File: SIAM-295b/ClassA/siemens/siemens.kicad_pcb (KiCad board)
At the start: 2 copper layers, 100 x 100 mm, 107 parts, among them J1 PWR_IN, J2 Conn_01x08_Pin, J3 AUDIO_IN, J4 AUDIO_OUT, Q1 BC849, Q10 BCX56, Q11 BCX56, Q12 BC849, Q2 BCX56, Q3 BCX56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

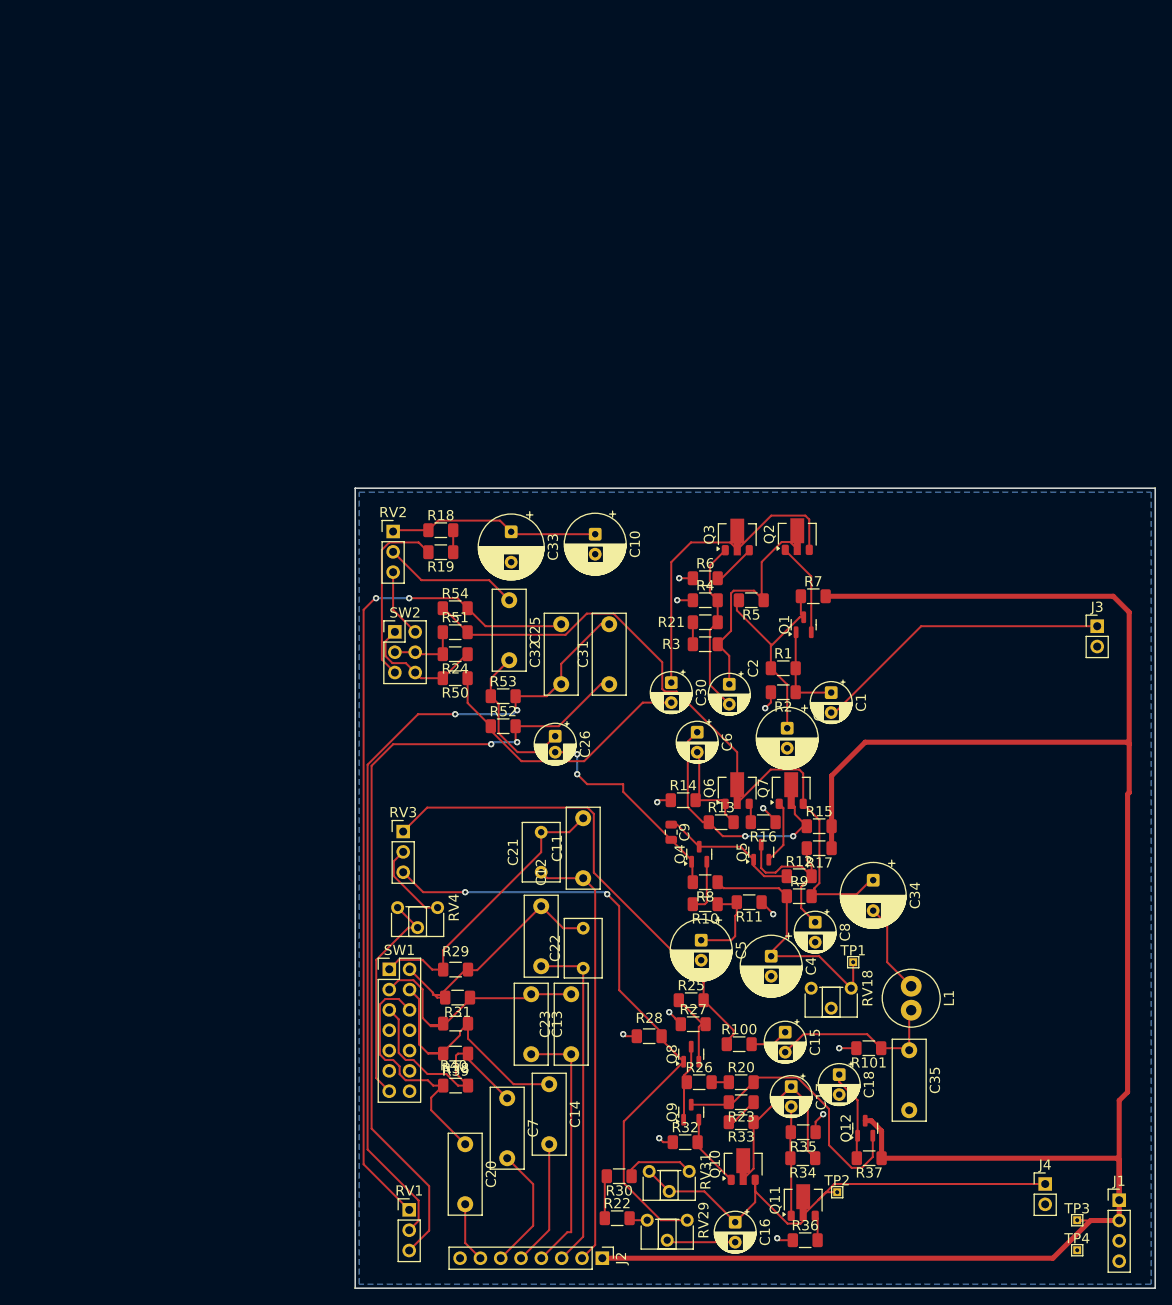
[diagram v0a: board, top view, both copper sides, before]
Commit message: update ocb
added mounting holes, reduced width
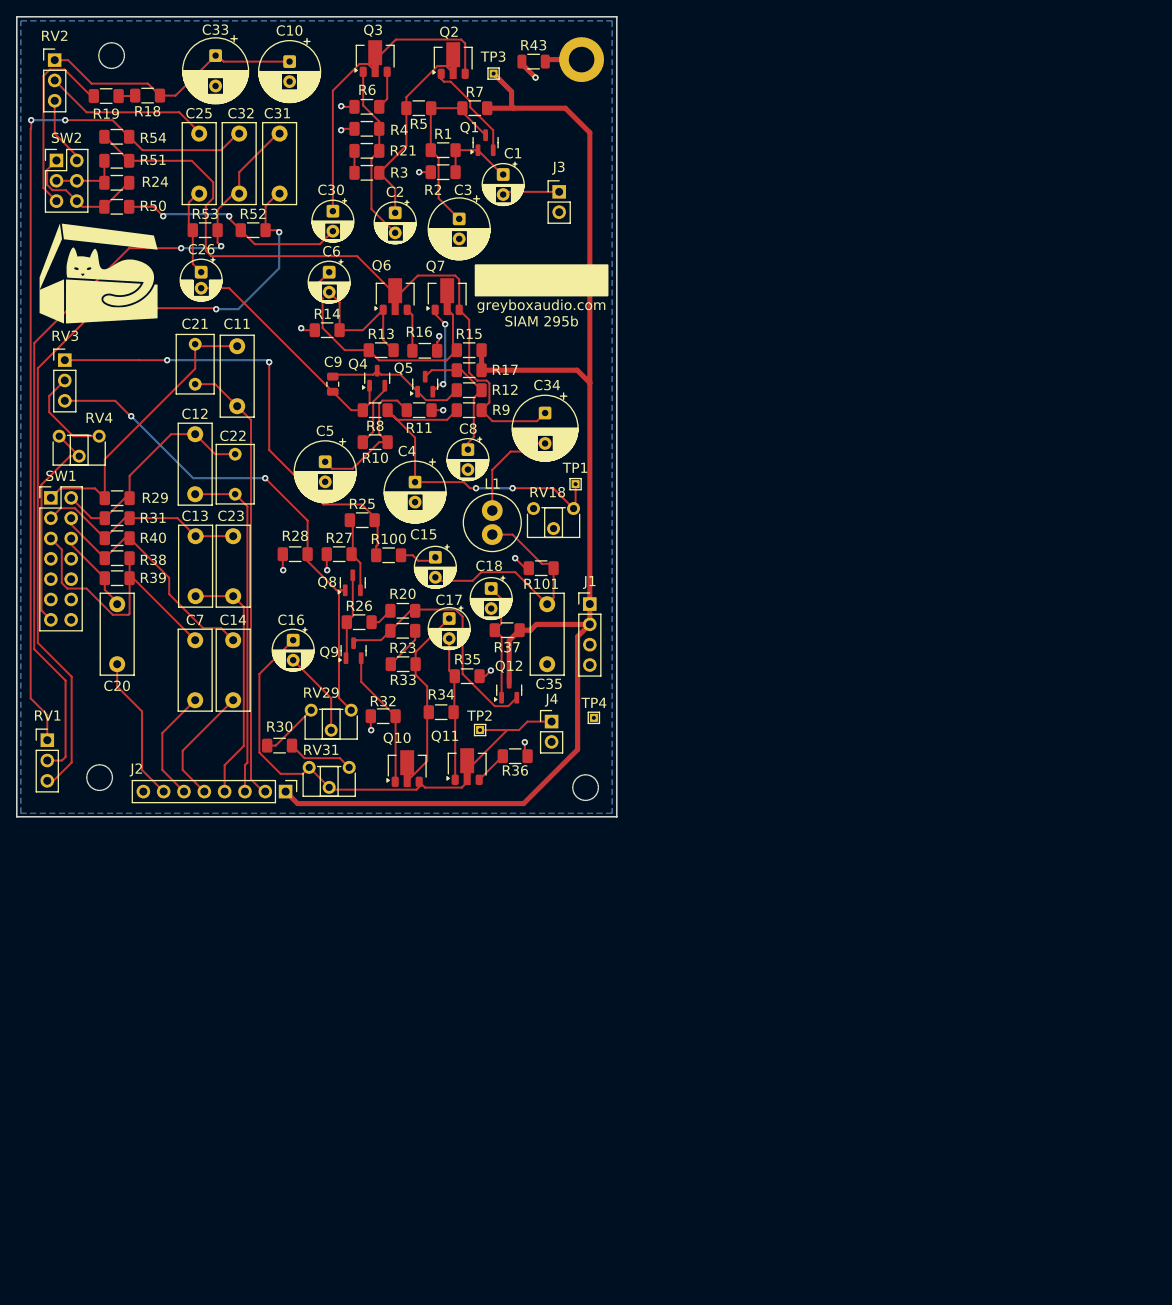
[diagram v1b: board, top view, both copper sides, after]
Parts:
- removed R22: 1k2, Resistor_SMD:R_1206_3216Metric_Pad1.30x1.75mm_HandSolder
- added G***: LOGO, LOGO, F.Cu at (35.8, 57.5)
- added H1: MountingHole, MountingHole:MountingHole_3.2mm_M3_DIN965, F.Cu at (37.2, 30.2)
- added H2: MountingHole, MountingHole:MountingHole_3.2mm_M3_DIN965, F.Cu at (35.8, 120.5)
- added H3: MountingHole, MountingHole:MountingHole_3.2mm_M3_DIN965_Pad, F.Cu at (96.0, 30.8)
- added H4: MountingHole, MountingHole:MountingHole_3.2mm_M3_DIN965, F.Cu at (96.5, 121.8)
- added R43: 0R, Resistor_SMD:R_1206_3216Metric, F.Cu at (90.0, 31.0)
- R18: value 1k3 -> 2k4
- R19: value 1k2 -> 100R
- R30: value 1k2 -> 2k4
- moved TP3 160.8 mm to (85.0, 32.5)
- moved J1 99.7 mm to (97.0, 98.8)
- moved C16 91.4 mm to (59.9, 103.3)
- moved TP4 89.9 mm to (97.5, 113.0)
- moved J3 86.4 mm to (93.2, 47.3)
- moved J4 84.5 mm to (92.2, 113.5)
- moved C20 80.3 mm to (37.9, 98.8)
- moved R37 80.0 mm to (86.7, 102.1)
- moved L1 79.2 mm to (84.8, 87.1)
- moved R2 77.7 mm to (78.7, 44.8)
- moved R1 77.5 mm to (78.7, 42.1)
- moved C1 76.6 mm to (86.2, 45.1)
- moved RV29 76.3 mm to (67.2, 112.1)
- moved R39 76.2 mm to (37.9, 95.6)
- moved C5 76.1 mm to (63.9, 81.0)
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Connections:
- R30 pad 2: Net-(R22-Pad1) -> Net-(R30-Pad2)
- RV29 pad 3: Net-(R22-Pad2) -> Net-(R30-Pad2)
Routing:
- net +24V: track 276.0 -> 170.0 mm
- net Net-(J3-Pin_1): track 37.3 -> 6.67 mm
- net Net-(C20-Pad1): track 30.6 -> 10.3 mm
- net Net-(Q8-B): track 78.8 -> 63.4 mm
- net Net-(C4-Pad1): track 31.8 -> 43.0 mm, vias 0 -> 2
- net Net-(J2-Pin_7): track 7.54 -> 18.3 mm
- net Net-(C25-Pad2): track 19.4 -> 10.2 mm
- net Net-(Q10-B): track 8.60 -> 17.2 mm
- net Net-(C15-Pad2): track 21.7 -> 29.9 mm
- net Net-(C5-Pad1): track 10.9 -> 18.9 mm
- net Net-(C10-Pad1): track 25.9 -> 33.3 mm
- net Net-(R30-Pad2): track 0.00 -> 7.33 mm
- net Net-(C30-Pad2): track 34.4 -> 28.5 mm, vias 0 -> 2
- net Net-(Q6-B): track 11.9 -> 17.4 mm
- net Net-(C7-Pad1): track 29.1 -> 34.2 mm
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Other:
- board size 100 x 100 mm -> 75 x 100 mm
- board text added: "greyboxaudio.com SIAM 295b"

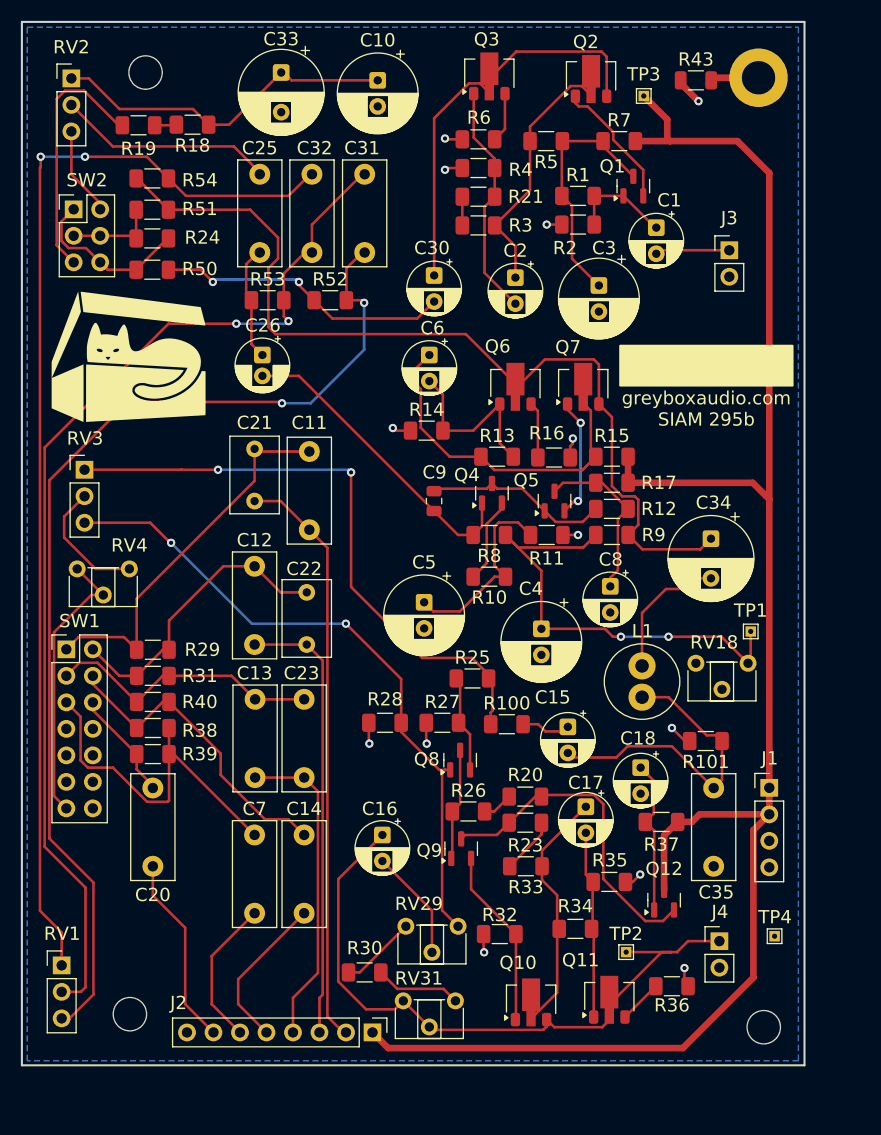
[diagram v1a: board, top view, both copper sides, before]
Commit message: update & fab
updated pcb, added fabrication output
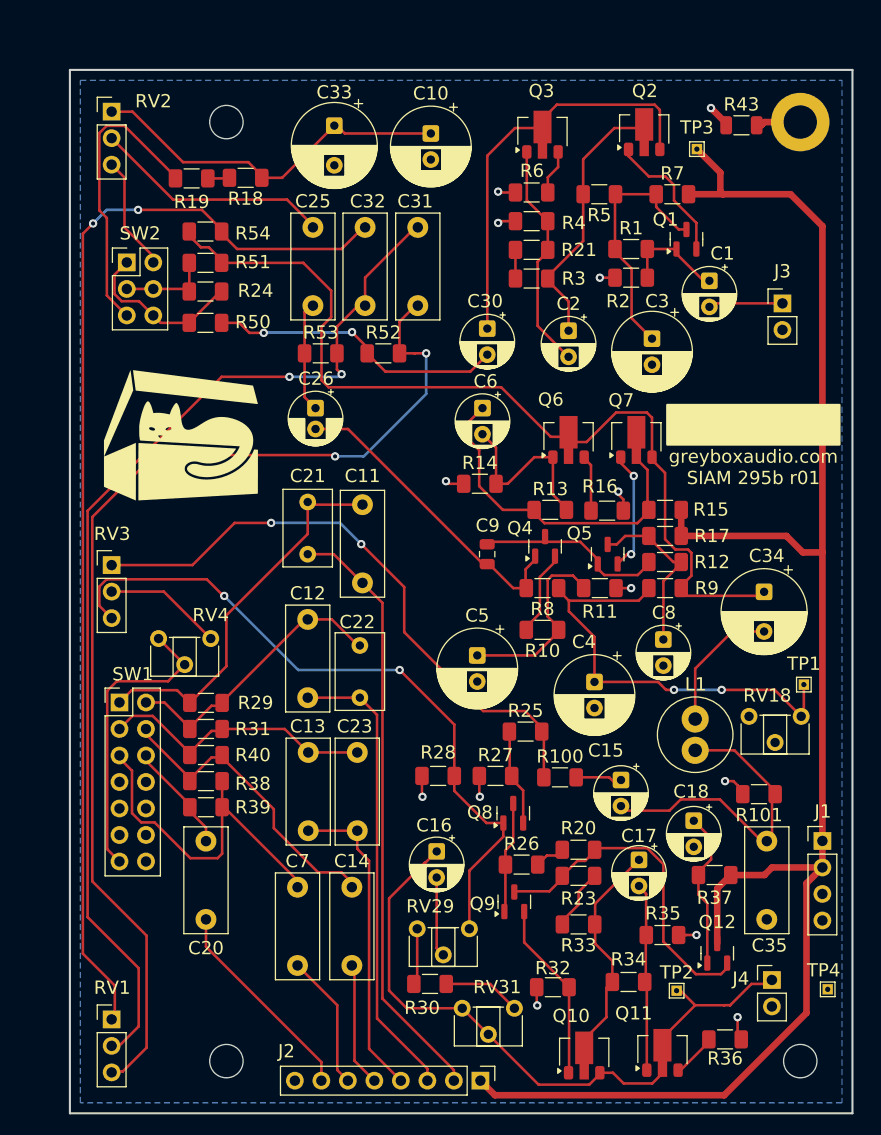
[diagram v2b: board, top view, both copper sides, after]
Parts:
- moved J2 11.3 mm to (69.3, 126.9)
- moved H2 10.3 mm to (45.0, 125.0)
- moved RV4 10.3 mm to (43.5, 84.5)
- moved RV3 9.50 mm to (34.0, 77.5)
- moved H1 9.09 mm to (45.0, 35.0)
- moved G*** 9.04 mm to (40.8, 65.0)
- moved Q3 7.56 mm to (75.3, 35.9)
- moved R33 7.52 mm to (78.8, 111.9)
- moved R100 7.20 mm to (77.0, 97.8)
- moved TP1 7.20 mm to (100.3, 88.9)
- moved C11 7.20 mm to (58.0, 79.2)
- moved C12 7.20 mm to (52.8, 82.7)
- moved C20 7.20 mm to (43.0, 103.9)
- moved C21 7.20 mm to (52.8, 76.4)
- moved C22 7.20 mm to (57.8, 90.2)
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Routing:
- net +24V: track 170.0 -> 163.5 mm
- net Net-(Q8-B): track 63.4 -> 67.2 mm
- net Net-(SW2B-B): track 24.0 -> 27.7 mm
- net Net-(J2-Pin_5): track 15.2 -> 11.5 mm
- net Net-(C31-Pad1): track 102.0 -> 105.7 mm
- net Net-(C16-Pad2): track 10.7 -> 7.68 mm
- net Net-(Q10-C): track 23.7 -> 20.7 mm
- net Net-(SW2A-B): track 8.02 -> 10.4 mm
- net Net-(C12-Pad1): track 28.6 -> 26.2 mm
- net Net-(R30-Pad2): track 7.33 -> 4.97 mm
- net Net-(C25-Pad1): track 20.7 -> 22.8 mm
- net Net-(C14-Pad1): track 30.3 -> 28.4 mm
- net Net-(C10-Pad1): track 33.3 -> 35.3 mm
- net Net-(Q6-C): track 88.0 -> 86.1 mm
- net Net-(J2-Pin_2): track 55.9 -> 57.7 mm
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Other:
- board text added: "greyboxaudio.com SIAM 295b r01"
- board text removed: "greyboxaudio.com SIAM 295b"

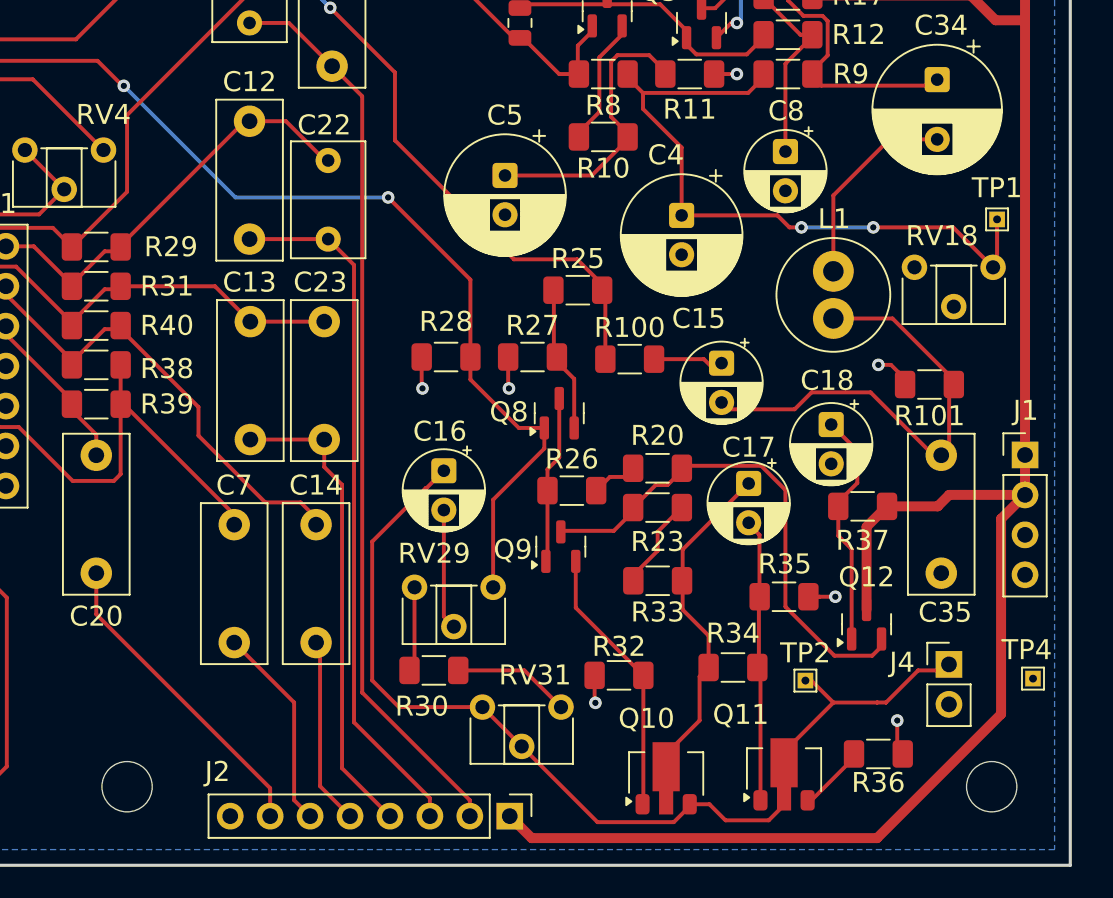
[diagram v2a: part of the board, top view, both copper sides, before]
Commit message: update pcb
added thermal realief for Q10/11, increased spacing for larger trim potentiometer footprints
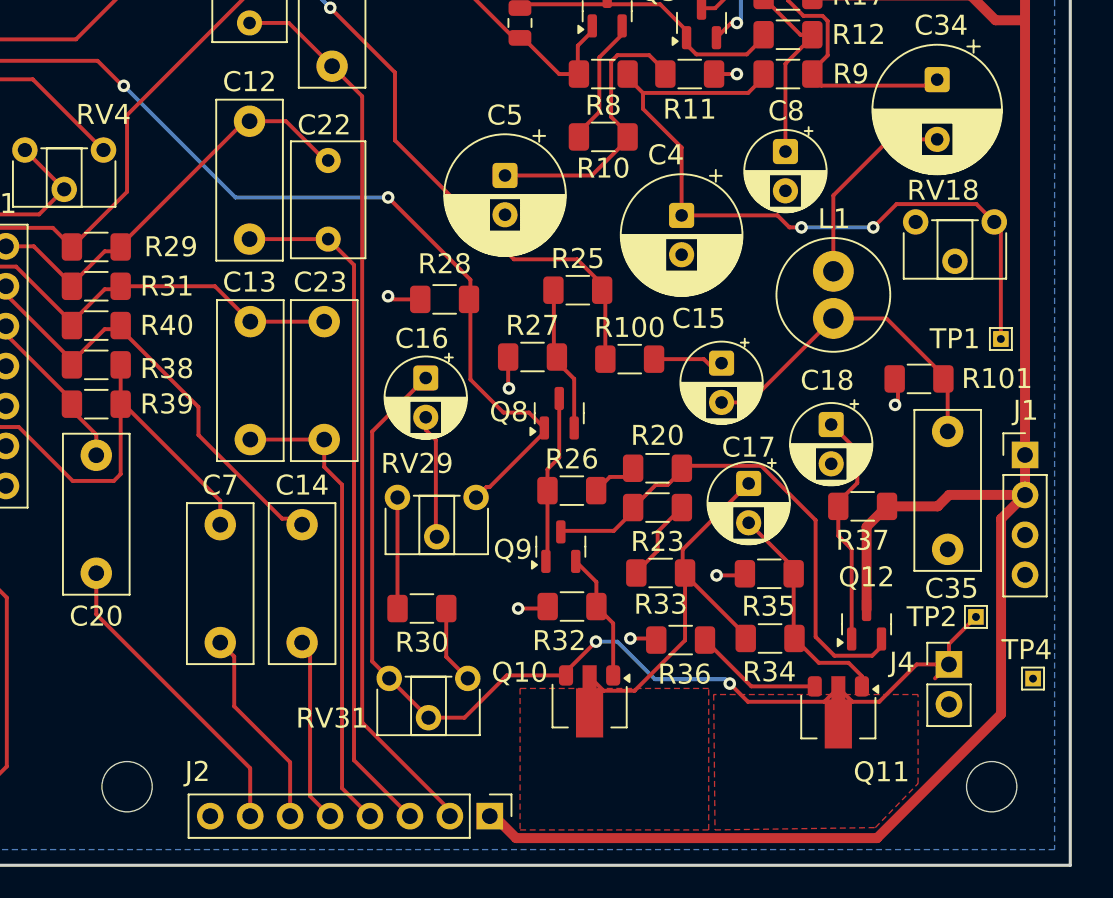
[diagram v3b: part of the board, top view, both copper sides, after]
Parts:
- moved R36 14.5 mm to (80.2, 115.7), turned to 0 degrees
- moved TP2 11.6 mm to (99.0, 114.2)
- moved TP1 7.61 mm to (100.6, 96.5)
- moved Q10 6.49 mm to (74.4, 119.9), turned to -90 degrees
- moved RV31 6.20 mm to (66.7, 118.1)
- moved C16 6.01 mm to (64.0, 99.0)
- moved RV29 5.82 mm to (67.2, 106.6)
- moved R32 5.30 mm to (73.3, 113.5)
- moved Q11 4.81 mm to (90.2, 120.6), turned to -90 degrees
- moved R30 4.01 mm to (63.8, 113.7)
- moved R28 3.67 mm to (65.2, 94.0)
- moved R34 3.00 mm to (85.9, 115.6)
- moved RV18 2.89 mm to (100.2, 89.1)
- moved R35 1.74 mm to (85.9, 111.5), turned to 0 degrees
- moved C35 1.57 mm to (97.2, 102.4)
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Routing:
- net Net-(Q10-B): track 17.2 -> 8.24 mm
- net Net-(J4-Pin_1): track 61.5 -> 67.8 mm, vias 0 -> 2
- net Net-(C15-Pad2): track 28.1 -> 21.9 mm
- net Net-(Q8-B): track 67.2 -> 61.6 mm
- net Net-(Q11-E): track 3.83 -> 8.20 mm
- net Net-(C4-Pad1): track 42.2 -> 46.6 mm
- net Net-(Q10-C): track 20.7 -> 24.8 mm
- net Net-(Q11-B): track 17.5 -> 14.0 mm
- net Net-(R30-Pad1): track 7.50 -> 5.01 mm
- net Net-(R30-Pad2): track 4.97 -> 7.06 mm
- net Net-(C14-Pad1): track 28.4 -> 27.0 mm
- net +24V: track 163.5 -> 164.5 mm
- net Net-(J2-Pin_3): track 44.4 -> 43.5 mm
- net Net-(J2-Pin_4): track 30.4 -> 29.5 mm
- net Net-(J2-Pin_5): track 11.5 -> 10.7 mm
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- added copper zone on F.Cu, net Net-(J4-Pin_1)
- added copper zone on F.Cu, net Net-(Q10-C)
